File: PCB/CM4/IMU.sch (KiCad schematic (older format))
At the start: 8 parts, among them U2 MPU6000, U3 HMC5883L, U4 BMP085

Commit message: altimeter caps
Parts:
- added C12: 0.1uF, 0603, symbol C
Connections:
- net +3.3V: now also U4.3 (VDDA), U4.4 (VDDD), C12.1
- net GND: now also U4.1 (GND), C12.2
- net SCL: now also U4.6 (SCL)
- net SDA: now also U4.7 (SDA)
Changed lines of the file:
@@
-EESchema Schematic File Version 2  date Sun 04 Nov 2012 06:51:49 PM COT
+EESchema Schematic File Version 2  date Sun 04 Nov 2012 07:09:00 PM COT
 LIBS:power
 LIBS:device
@@
 Sheet 2 3
 Title ""
-Date "4 nov 2012"
+Date "5 nov 2012"
 Rev ""
 Comp ""
@@
 $EndComp
 $Comp
-L +3.3V #PWR01
+L +3.3V #PWR12
 U 1 1 5095AC9D
 P 8250 3600
-F 0 "#PWR01" H 8250 3560 30  0001 C CNN
+F 0 "#PWR12" H 8250 3560 30  0001 C CNN
 F 1 "+3.3V" H 8250 3710 30  0000 C CNN
 	1    8250 3600
@@
 $EndComp
 $Comp
-L GND #PWR02
+L GND #PWR14
 U 1 1 5095ACAC
 P 8600 3700
-F 0 "#PWR02" H 8600 3700 30  0001 C CNN
+F 0 "#PWR14" H 8600 3700 30  0001 C CNN
 F 1 "GND" H 8600 3630 30  0001 C CNN
 	1    8600 3700
@@
 $EndComp
 $Comp
-L GND #PWR03
+L GND #PWR11
 U 1 1 5095ACB9
 P 8250 3250
-F 0 "#PWR03" H 8250 3250 30  0001 C CNN
+F 0 "#PWR11" H 8250 3250 30  0001 C CNN
 F 1 "GND" H 8250 3180 30  0001 C CNN
 	1    8250 3250
@@
 $EndComp
 $Comp
-L +3.3V #PWR04
+L +3.3V #PWR13
 U 1 1 5095ACEB
 P 8600 3100
-F 0 "#PWR04" H 8600 3060 30  0001 C CNN
+F 0 "#PWR13" H 8600 3060 30  0001 C CNN
 F 1 "+3.3V" H 8600 3210 30  0000 C CNN
 	1    8600 3100
@@
 	7400 1800 7400 1900
 $Comp
-L GND #PWR05
+L GND #PWR10
 U 1 1 5095AEE9
 P 7700 1900
-F 0 "#PWR05" H 7700 1900 30  0001 C CNN
+F 0 "#PWR10" H 7700 1900 30  0001 C CNN
 F 1 "GND" H 7700 1830 30  0001 C CNN
 	1    7700 1900
@@
 $EndComp
 $Comp
-L GND #PWR06
+L GND #PWR9
 U 1 1 5095AFB5
 P 7300 4900
-F 0 "#PWR06" H 7300 4900 30  0001 C CNN
+F 0 "#PWR9" H 7300 4900 30  0001 C CNN
 F 1 "GND" H 7300 4830 30  0001 C CNN
 	1    7300 4900
@@
 $EndComp
 $Comp
-L GND #PWR07
+L GND #PWR6
 U 1 1 5095E346
 P 3750 5650
-F 0 "#PWR07" H 3750 5650 30  0001 C CNN
+F 0 "#PWR6" H 3750 5650 30  0001 C CNN
 F 1 "GND" H 3750 5580 30  0001 C CNN
 	1    3750 5650
@@
 $EndComp
 $Comp
-L +3.3V #PWR08
+L +3.3V #PWR5
 U 1 1 5095E352
 P 3750 5050
-F 0 "#PWR08" H 3750 5010 30  0001 C CNN
+F 0 "#PWR5" H 3750 5010 30  0001 C CNN
 F 1 "+3.3V" H 3750 5160 30  0000 C CNN
 	1    3750 5050
@@
 SCL
 $Comp
-L GND #PWR09
+L GND #PWR4
 U 1 1 5096F74E
 P 3000 5500
-F 0 "#PWR09" H 3000 5500 30  0001 C CNN
+F 0 "#PWR4" H 3000 5500 30  0001 C CNN
 F 1 "GND" H 3000 5430 30  0001 C CNN
 	1    3000 5500
@@
 Connection ~ 3000 5450
 $Comp
-L +3.3V #PWR010
+L +3.3V #PWR1
 U 1 1 5096F8D1
 P 2300 4500
-F 0 "#PWR010" H 2300 4460 30  0001 C CNN
+F 0 "#PWR1" H 2300 4460 30  0001 C CNN
 F 1 "+3.3V" H 2300 4610 30  0000 C CNN
 	1    2300 4500
@@
 Text Notes 6450 1550 0    60   ~ 0
 3-AXIS GYRO, 3-AXIS ACCEL
+Wire Wire Line
+	1950 1700 1750 1700
+Text HLabel 1750 1700 0    60   Input ~ 0
+SCL
+Text HLabel 1750 1800 0    60   BiDi ~ 0
+SDA
+Wire Wire Line
+	1750 1800 1950 1800
+$Comp
+L +3.3V #PWR2
+U 1 1 5097041F
+P 2600 1000
+F 0 "#PWR2" H 2600 960 30  0001 C CNN
+F 1 "+3.3V" H 2600 1110 30  0000 C CNN
+	1    2600 1000
+	1    0    0    -1
+$EndComp
+$Comp
+L GND #PWR8
+U 1 1 50970425
+P 3950 2450
+F 0 "#PWR8" H 3950 2450 30  0001 C CNN
+F 1 "GND" H 3950 2380 30  0001 C CNN
+	1    3950 2450
+	1    0    0    -1
+$EndComp
+$Comp
+L C C12
+U 1 1 5097042B
+P 3950 2150
+F 0 "C12" H 4000 2250 50  0000 L CNN
+F 1 "0.1uF" H 4000 2050 50  0000 L CNN
+F 2 "0603" H 3950 2150 60  0001 C CNN
+	1    3950 2150
+	1    0    0    -1
+$EndComp
+Wire Wire Line
+	3950 2350 3950 2450
+$Comp
+L GND #PWR3
+U 1 1 50970433
+P 2600 2750
+F 0 "#PWR3" H 2600 2750 30  0001 C CNN
+F 1 "GND" H 2600 2680 30  0001 C CNN
+	1    2600 2750
+	1    0    0    -1
+$EndComp
+Wire Wire Line
+	2600 2650 2600 2750
+$Comp
+L +3.3V #PWR7
+U 1 1 5097043A
+P 3950 1900
+F 0 "#PWR7" H 3950 1860 30  0001 C CNN
+F 1 "+3.3V" H 3950 2010 30  0000 C CNN
+	1    3950 1900
+	1    0    0    -1
+$EndComp
+Wire Wire Line
+	2600 1000 2600 1050
+Wire Wire Line
+	2550 1050 2650 1050
+Wire Wire Line
+	2550 1050 2550 1150
+Wire Wire Line
+	2650 1050 2650 1150
+Connection ~ 2600 1050
+Wire Wire Line
+	3950 1900 3950 1950
 $EndSCHEMATC

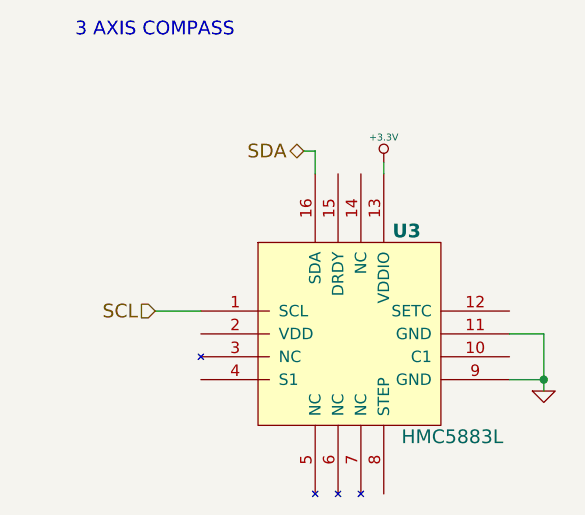
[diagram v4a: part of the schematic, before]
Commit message: changing SPI Cortex M4 portd
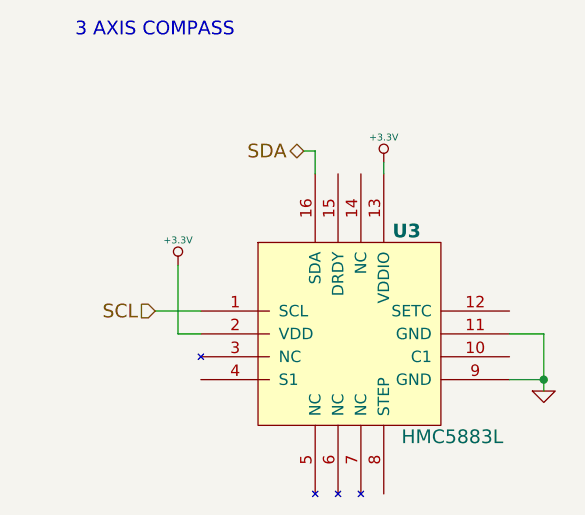
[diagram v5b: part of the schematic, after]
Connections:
- net +3.3V: now also U3.2 (VDD)
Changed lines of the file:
@@
-EESchema Schematic File Version 2  date Sun 04 Nov 2012 07:09:00 PM COT
+EESchema Schematic File Version 2  date Sun 04 Nov 2012 10:48:55 PM COT
 LIBS:power
 LIBS:device
@@
 LIBS:bmp085
 LIBS:HackBo_DroneCore_CM4-cache
-EELAYER 25  0
+EELAYER 27 0
 EELAYER END
 $Descr A4 11693 8268
@@
 $EndComp
 $Comp
-L +3.3V #PWR12
+L +3.3V #PWR01
 U 1 1 5095AC9D
 P 8250 3600
-F 0 "#PWR12" H 8250 3560 30  0001 C CNN
+F 0 "#PWR01" H 8250 3560 30  0001 C CNN
 F 1 "+3.3V" H 8250 3710 30  0000 C CNN
 	1    8250 3600
@@
 $EndComp
 $Comp
-L GND #PWR14
+L GND #PWR02
 U 1 1 5095ACAC
 P 8600 3700
-F 0 "#PWR14" H 8600 3700 30  0001 C CNN
+F 0 "#PWR02" H 8600 3700 30  0001 C CNN
 F 1 "GND" H 8600 3630 30  0001 C CNN
 	1    8600 3700
@@
 $EndComp
 $Comp
-L GND #PWR11
+L GND #PWR03
 U 1 1 5095ACB9
 P 8250 3250
-F 0 "#PWR11" H 8250 3250 30  0001 C CNN
+F 0 "#PWR03" H 8250 3250 30  0001 C CNN
 F 1 "GND" H 8250 3180 30  0001 C CNN
 	1    8250 3250
@@
 $EndComp
 $Comp
-L +3.3V #PWR13
+L +3.3V #PWR04
 U 1 1 5095ACEB
 P 8600 3100
-F 0 "#PWR13" H 8600 3060 30  0001 C CNN
+F 0 "#PWR04" H 8600 3060 30  0001 C CNN
 F 1 "+3.3V" H 8600 3210 30  0000 C CNN
 	1    8600 3100
@@
 	7400 1800 7400 1900
 $Comp
-L GND #PWR10
+L GND #PWR05
 U 1 1 5095AEE9
 P 7700 1900
-F 0 "#PWR10" H 7700 1900 30  0001 C CNN
+F 0 "#PWR05" H 7700 1900 30  0001 C CNN
 F 1 "GND" H 7700 1830 30  0001 C CNN
 	1    7700 1900
@@
 $EndComp
 $Comp
-L GND #PWR9
+L GND #PWR06
 U 1 1 5095AFB5
 P 7300 4900
-F 0 "#PWR9" H 7300 4900 30  0001 C CNN
+F 0 "#PWR06" H 7300 4900 30  0001 C CNN
 F 1 "GND" H 7300 4830 30  0001 C CNN
 	1    7300 4900
@@
 $EndComp
 $Comp
-L GND #PWR6
+L GND #PWR07
 U 1 1 5095E346
 P 3750 5650
-F 0 "#PWR6" H 3750 5650 30  0001 C CNN
+F 0 "#PWR07" H 3750 5650 30  0001 C CNN
 F 1 "GND" H 3750 5580 30  0001 C CNN
 	1    3750 5650
@@
 $EndComp
 $Comp
-L +3.3V #PWR5
+L +3.3V #PWR08
 U 1 1 5095E352
 P 3750 5050
-F 0 "#PWR5" H 3750 5010 30  0001 C CNN
+F 0 "#PWR08" H 3750 5010 30  0001 C CNN
 F 1 "+3.3V" H 3750 5160 30  0000 C CNN
 	1    3750 5050
@@
 SCL
 $Comp
-L GND #PWR4
+L GND #PWR09
 U 1 1 5096F74E
 P 3000 5500
-F 0 "#PWR4" H 3000 5500 30  0001 C CNN
+F 0 "#PWR09" H 3000 5500 30  0001 C CNN
 F 1 "GND" H 3000 5430 30  0001 C CNN
 	1    3000 5500
@@
 Connection ~ 3000 5450
 $Comp
-L +3.3V #PWR1
+L +3.3V #PWR010
 U 1 1 5096F8D1
 P 2300 4500
-F 0 "#PWR1" H 2300 4460 30  0001 C CNN
+F 0 "#PWR010" H 2300 4460 30  0001 C CNN
 F 1 "+3.3V" H 2300 4610 30  0000 C CNN
 	1    2300 4500
@@
 	1750 1800 1950 1800
 $Comp
-L +3.3V #PWR2
+L +3.3V #PWR011
 U 1 1 5097041F
 P 2600 1000
-F 0 "#PWR2" H 2600 960 30  0001 C CNN
+F 0 "#PWR011" H 2600 960 30  0001 C CNN
 F 1 "+3.3V" H 2600 1110 30  0000 C CNN
 	1    2600 1000
@@
 $EndComp
 $Comp
-L GND #PWR8
+L GND #PWR012
 U 1 1 50970425
 P 3950 2450
-F 0 "#PWR8" H 3950 2450 30  0001 C CNN
+F 0 "#PWR012" H 3950 2450 30  0001 C CNN
 F 1 "GND" H 3950 2380 30  0001 C CNN
 	1    3950 2450
@@
 	3950 2350 3950 2450
 $Comp
-L GND #PWR3
+L GND #PWR013
 U 1 1 50970433
 P 2600 2750
-F 0 "#PWR3" H 2600 2750 30  0001 C CNN
+F 0 "#PWR013" H 2600 2750 30  0001 C CNN
 F 1 "GND" H 2600 2680 30  0001 C CNN
 	1    2600 2750
@@
 	2600 2650 2600 2750
 $Comp
-L +3.3V #PWR7
+L +3.3V #PWR014
 U 1 1 5097043A
 P 3950 1900
-F 0 "#PWR7" H 3950 1860 30  0001 C CNN
+F 0 "#PWR014" H 3950 1860 30  0001 C CNN
 F 1 "+3.3V" H 3950 2010 30  0000 C CNN
 	1    3950 1900
@@
 Wire Wire Line
 	3950 1900 3950 1950
+$Comp
+L +3.3V #PWR?
+U 1 1 50973854
+P 1400 4950
+F 0 "#PWR?" H 1400 4910 30  0001 C CNN
+F 1 "+3.3V" H 1400 5060 30  0000 C CNN
+	1    1400 4950
+	1    0    0    -1
+$EndComp
+Wire Wire Line
+	1400 4950 1400 5250
+Wire Wire Line
+	1400 5250 1500 5250
 $EndSCHEMATC

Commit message: replacemnt
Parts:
- added C15, C16: 10uF, 0805, symbol C
- added C17: 0.1uF, 0603, symbol C
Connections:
- net +3.3V: now also C15.1, C16.1, C17.1
- net GND: now also U2.PAD (GND), C15.2, C16.2, C17.2
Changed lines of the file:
@@
-EESchema Schematic File Version 2  date Sun 04 Nov 2012 10:48:55 PM COT
+EESchema Schematic File Version 2  date Mon 05 Nov 2012 06:52:04 AM COT
 LIBS:power
 LIBS:device
@@
 LIBS:mpu6050
 LIBS:stm32f100vxx
-LIBS:mpu6000
 LIBS:hmc5883l
 LIBS:bmp085
+LIBS:mpu6000
 LIBS:HackBo_DroneCore_CM4-cache
 EELAYER 27 0
@@
 $EndDescr
 $Comp
-L MPU6000 U2
-U 1 1 5095AB32
-P 7150 3350
-F 0 "U2" H 6700 3900 60  0000 C CNB
-F 1 "MPU6000" H 7150 3350 60  0000 C CNB
-F 2 "QFN24P" H 7150 3350 60  0001 C CNN
-	1    7150 3350
-	1    0    0    -1
-$EndComp
-$Comp
-L +3.3V #PWR01
+L +3.3V #PWR14
 U 1 1 5095AC9D
 P 8250 3600
-F 0 "#PWR01" H 8250 3560 30  0001 C CNN
+F 0 "#PWR14" H 8250 3560 30  0001 C CNN
 F 1 "+3.3V" H 8250 3710 30  0000 C CNN
 	1    8250 3600
@@
 $EndComp
 $Comp
-L GND #PWR02
+L GND #PWR16
 U 1 1 5095ACAC
 P 8600 3700
-F 0 "#PWR02" H 8600 3700 30  0001 C CNN
+F 0 "#PWR16" H 8600 3700 30  0001 C CNN
 F 1 "GND" H 8600 3630 30  0001 C CNN
 	1    8600 3700
@@
 $EndComp
 $Comp
-L GND #PWR03
+L GND #PWR13
 U 1 1 5095ACB9
 P 8250 3250
-F 0 "#PWR03" H 8250 3250 30  0001 C CNN
+F 0 "#PWR13" H 8250 3250 30  0001 C CNN
 F 1 "GND" H 8250 3180 30  0001 C CNN
 	1    8250 3250
@@
 $EndComp
 $Comp
-L +3.3V #PWR04
+L +3.3V #PWR15
 U 1 1 5095ACEB
 P 8600 3100
-F 0 "#PWR04" H 8600 3060 30  0001 C CNN
+F 0 "#PWR15" H 8600 3060 30  0001 C CNN
 F 1 "+3.3V" H 8600 3210 30  0000 C CNN
 	1    8600 3100
@@
 	7400 1800 7400 1900
 $Comp
-L GND #PWR05
+L GND #PWR11
 U 1 1 5095AEE9
 P 7700 1900
-F 0 "#PWR05" H 7700 1900 30  0001 C CNN
+F 0 "#PWR11" H 7700 1900 30  0001 C CNN
 F 1 "GND" H 7700 1830 30  0001 C CNN
 	1    7700 1900
@@
 $EndComp
 $Comp
-L GND #PWR06
+L GND #PWR10
 U 1 1 5095AFB5
 P 7300 4900
-F 0 "#PWR06" H 7300 4900 30  0001 C CNN
+F 0 "#PWR10" H 7300 4900 30  0001 C CNN
 F 1 "GND" H 7300 4830 30  0001 C CNN
 	1    7300 4900
@@
 $EndComp
 $Comp
-L GND #PWR07
+L GND #PWR7
 U 1 1 5095E346
 P 3750 5650
-F 0 "#PWR07" H 3750 5650 30  0001 C CNN
+F 0 "#PWR7" H 3750 5650 30  0001 C CNN
 F 1 "GND" H 3750 5580 30  0001 C CNN
 	1    3750 5650
@@
 $EndComp
 $Comp
-L +3.3V #PWR08
+L +3.3V #PWR6
 U 1 1 5095E352
 P 3750 5050
-F 0 "#PWR08" H 3750 5010 30  0001 C CNN
+F 0 "#PWR6" H 3750 5010 30  0001 C CNN
 F 1 "+3.3V" H 3750 5160 30  0000 C CNN
 	1    3750 5050
@@
 SCL
 $Comp
-L GND #PWR09
+L GND #PWR5
 U 1 1 5096F74E
 P 3000 5500
-F 0 "#PWR09" H 3000 5500 30  0001 C CNN
+F 0 "#PWR5" H 3000 5500 30  0001 C CNN
 F 1 "GND" H 3000 5430 30  0001 C CNN
 	1    3000 5500
@@
 Connection ~ 3000 5450
 $Comp
-L +3.3V #PWR010
+L +3.3V #PWR2
 U 1 1 5096F8D1
 P 2300 4500
-F 0 "#PWR010" H 2300 4460 30  0001 C CNN
+F 0 "#PWR2" H 2300 4460 30  0001 C CNN
 F 1 "+3.3V" H 2300 4610 30  0000 C CNN
 	1    2300 4500
@@
 	1750 1800 1950 1800
 $Comp
-L +3.3V #PWR011
+L +3.3V #PWR3
 U 1 1 5097041F
 P 2600 1000
-F 0 "#PWR011" H 2600 960 30  0001 C CNN
+F 0 "#PWR3" H 2600 960 30  0001 C CNN
 F 1 "+3.3V" H 2600 1110 30  0000 C CNN
 	1    2600 1000
@@
 $EndComp
 $Comp
-L GND #PWR012
+L GND #PWR9
 U 1 1 50970425
 P 3950 2450
-F 0 "#PWR012" H 3950 2450 30  0001 C CNN
+F 0 "#PWR9" H 3950 2450 30  0001 C CNN
 F 1 "GND" H 3950 2380 30  0001 C CNN
 	1    3950 2450
@@
 	3950 2350 3950 2450
 $Comp
-L GND #PWR013
+L GND #PWR4
 U 1 1 50970433
 P 2600 2750
-F 0 "#PWR013" H 2600 2750 30  0001 C CNN
+F 0 "#PWR4" H 2600 2750 30  0001 C CNN
 F 1 "GND" H 2600 2680 30  0001 C CNN
 	1    2600 2750
@@
 	2600 2650 2600 2750
 $Comp
-L +3.3V #PWR014
+L +3.3V #PWR8
 U 1 1 5097043A
 P 3950 1900
-F 0 "#PWR014" H 3950 1860 30  0001 C CNN
+F 0 "#PWR8" H 3950 1860 30  0001 C CNN
 F 1 "+3.3V" H 3950 2010 30  0000 C CNN
 	1    3950 1900
@@
 	3950 1900 3950 1950
 $Comp
-L +3.3V #PWR?
+L +3.3V #PWR1
 U 1 1 50973854
 P 1400 4950
-F 0 "#PWR?" H 1400 4910 30  0001 C CNN
+F 0 "#PWR1" H 1400 4910 30  0001 C CNN
 F 1 "+3.3V" H 1400 5060 30  0000 C CNN
 	1    1400 4950
@@
 Wire Wire Line
 	1400 5250 1500 5250
+$Comp
+L MPU6000 U2
+U 1 1 5097A7E6
+P 7150 3350
+F 0 "U2" H 6700 3900 60  0000 C CNB
+F 1 "MPU6000" H 7150 3350 60  0000 C CNB
+F 2 "QFN24P" H 7150 3350 60  0001 C CNN
+	1    7150 3350
+	1    0    0    -1
+$EndComp
+$Comp
+L GND #PWR12
+U 1 1 5097A82F
+P 8050 3900
+F 0 "#PWR12" H 8050 3900 30  0001 C CNN
+F 1 "GND" H 8050 3830 30  0001 C CNN
+	1    8050 3900
+	1    0    0    -1
+$EndComp
+Wire Wire Line
+	8050 3800 8050 3900
+$Comp
+L GND #PWR18
+U 1 1 5097A9EC
+P 9850 1650
+F 0 "#PWR18" H 9850 1650 30  0001 C CNN
+F 1 "GND" H 9850 1580 30  0001 C CNN
+	1    9850 1650
+	1    0    0    -1
+$EndComp
+$Comp
+L C C15
+U 1 1 5097A9F2
+P 9850 1350
+F 0 "C15" H 9900 1450 50  0000 L CNN
+F 1 "10uF" H 9900 1250 50  0000 L CNN
+F 2 "0805" H 9850 1350 60  0001 C CNN
+	1    9850 1350
+	1    0    0    -1
+$EndComp
+$Comp
+L +3.3V #PWR17
+U 1 1 5097A9F8
+P 9850 1050
+F 0 "#PWR17" H 9850 1010 30  0001 C CNN
+F 1 "+3.3V" H 9850 1160 30  0000 C CNN
+	1    9850 1050
+	1    0    0    -1
+$EndComp
+Wire Wire Line
+	9850 1050 9850 1150
+Wire Wire Line
+	9850 1550 9850 1650
+$Comp
+L C C16
+U 1 1 5097AA0C
+P 10300 1350
+F 0 "C16" H 10350 1450 50  0000 L CNN
+F 1 "10uF" H 10350 1250 50  0000 L CNN
+F 2 "0805" H 10300 1350 60  0001 C CNN
+	1    10300 1350
+	1    0    0    -1
+$EndComp
+Wire Wire Line
+	9850 1100 10850 1100
+Wire Wire Line
+	10300 1100 10300 1150
+Connection ~ 9850 1100
+Wire Wire Line
+	9850 1600 10850 1600
+Wire Wire Line
+	10300 1600 10300 1550
+Connection ~ 9850 1600
+$Comp
+L C C17
+U 1 1 5097AA75
+P 10850 1350
+F 0 "C17" H 10900 1450 50  0000 L CNN
+F 1 "0.1uF" H 10900 1250 50  0000 L CNN
+F 2 "0603" H 10850 1350 60  0001 C CNN
+	1    10850 1350
+	1    0    0    -1
+$EndComp
+Wire Wire Line
+	10850 1100 10850 1150
+Connection ~ 10300 1100
+Wire Wire Line
+	10850 1600 10850 1550
+Connection ~ 10300 1600
 $EndSCHEMATC
